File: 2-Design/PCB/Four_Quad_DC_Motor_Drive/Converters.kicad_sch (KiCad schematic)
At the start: 0 parts

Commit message: Added the SQL50 symbol and footprint
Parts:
- added U?: SQL50, symbol ee463_symbol_library:SQL50
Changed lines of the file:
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@@
 (kicad_sch (version 20211123) (generator eeschema)
   (paper "A4")
+  (symbol (lib_id "ee463_symbol_library:SQL50") (at 105.41 97.79 0) (unit 1)
+    (in_bom yes) (on_board yes) (fields_autoplaced)
+    (property "Reference" "U?" (id 0) (at 105.41 85.09 0))
+    (property "Value" "SQL50" (id 1) (at 105.41 87.63 0))
+    (property "Footprint" "" (id 2) (at 105.41 97.79 0)
+      (effects (font (size 1.27 1.27)) hide)
+    )
+    (property "Datasheet" "" (id 3) (at 105.41 97.79 0)
+      (effects (font (size 1.27 1.27)) hide)
+    )
+    (pin "1")
+    (pin "2")
+    (pin "3")
+    (pin "4")
+    (pin "5")
+  )
 )

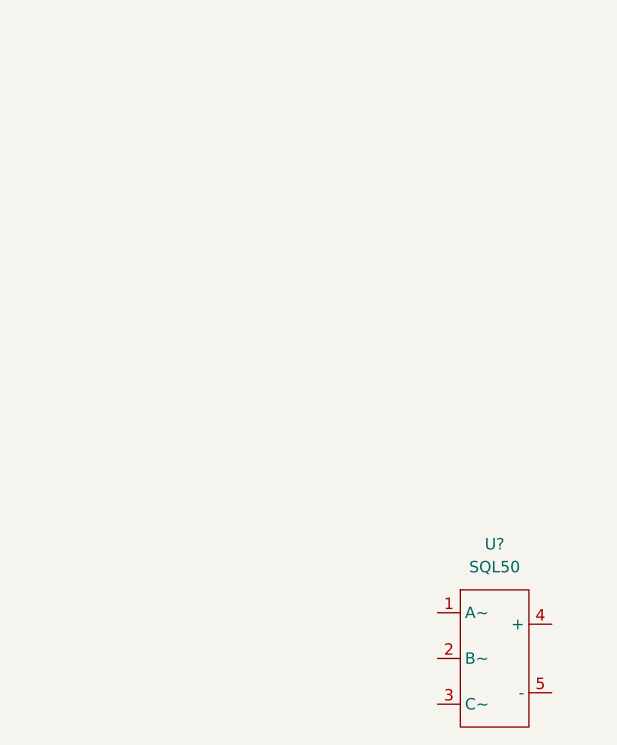
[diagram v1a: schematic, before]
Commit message: Added some more schematic symbols and three phase rectifier schematics
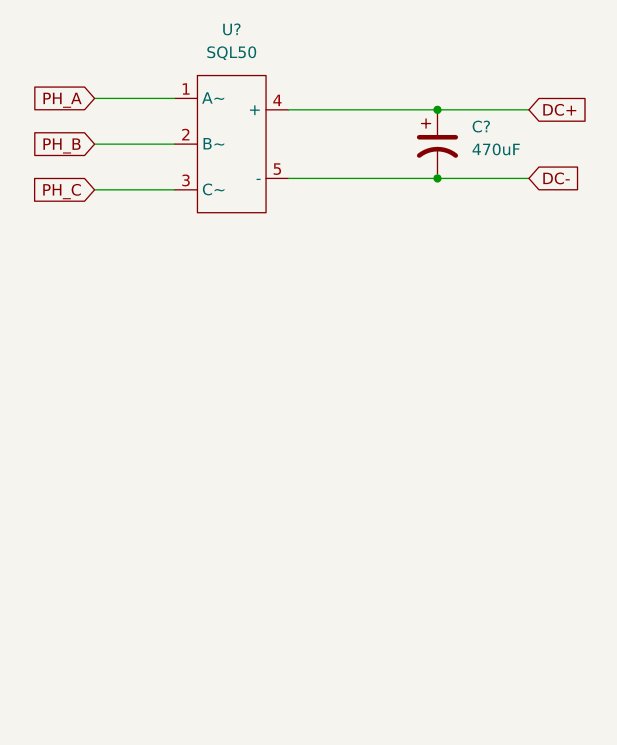
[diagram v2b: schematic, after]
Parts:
- added C?: 470uF, symbol Device:C_Polarized_US
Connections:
- net PH_A: now reaches U?.1 (A~)
- net PH_B: now reaches U?.2 (B~)
- net PH_C: now reaches U?.3 (C~)
- net DC+: now reaches U?.4 (+)
- net DC+: now also C?.1
- net DC-: now reaches U?.5 (-)
- net DC-: now also C?.2
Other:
- moved on the sheet: U?
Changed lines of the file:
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@@
 (kicad_sch (version 20211123) (generator eeschema)
   (paper "A4")
-  (symbol (lib_id "ee463_symbol_library:SQL50") (at 105.41 97.79 0) (unit 1)
+  (junction (at 99.06 36.83) (diameter 0) (color 0 0 0 0)
+  )
+  (junction (at 99.06 44.45) (diameter 0) (color 0 0 0 0)
+  )
+  (wire (pts (xy 60.96 45.72) (xy 69.85 45.72))
+    (stroke (width 0) (type default) (color 0 0 0 0))
+  )
+  (wire (pts (xy 82.55 44.45) (xy 99.06 44.45))
+    (stroke (width 0) (type default) (color 0 0 0 0))
+  )
+  (wire (pts (xy 99.06 36.83) (xy 109.22 36.83))
+    (stroke (width 0) (type default) (color 0 0 0 0))
+  )
+  (wire (pts (xy 60.96 35.56) (xy 69.85 35.56))
+    (stroke (width 0) (type default) (color 0 0 0 0))
+  )
+  (wire (pts (xy 99.06 44.45) (xy 109.22 44.45))
+    (stroke (width 0) (type default) (color 0 0 0 0))
+  )
+  (wire (pts (xy 82.55 36.83) (xy 99.06 36.83))
+    (stroke (width 0) (type default) (color 0 0 0 0))
+  )
+  (wire (pts (xy 60.96 40.64) (xy 69.85 40.64))
+    (stroke (width 0) (type default) (color 0 0 0 0))
+  )
+  (global_label "PH_C" (shape input) (at 60.96 45.72 180) (fields_autoplaced)
+    (effects (font (size 1.27 1.27)) (justify right))
+    (property "Intersheet References" "${INTERSHEET_REFS}" (id 0) (at 53.7088 45.6406 0)
+      (effects (font (size 1.27 1.27)) (justify right) hide)
+    )
+  )
+  (global_label "PH_A" (shape input) (at 60.96 35.56 180) (fields_autoplaced)
+    (effects (font (size 1.27 1.27)) (justify right))
+    (property "Intersheet References" "${INTERSHEET_REFS}" (id 0) (at 53.8902 35.4806 0)
+      (effects (font (size 1.27 1.27)) (justify right) hide)
+    )
+  )
+  (global_label "DC+" (shape input) (at 109.22 36.83 0) (fields_autoplaced)
+    (effects (font (size 1.27 1.27)) (justify left))
+    (property "Intersheet References" "${INTERSHEET_REFS}" (id 0) (at 115.7455 36.7506 0)
+      (effects (font (size 1.27 1.27)) (justify left) hide)
+    )
+  )
+  (global_label "DC-" (shape input) (at 109.22 44.45 0) (fields_autoplaced)
+    (effects (font (size 1.27 1.27)) (justify left))
+    (property "Intersheet References" "${INTERSHEET_REFS}" (id 0) (at 115.7455 44.3706 0)
+      (effects (font (size 1.27 1.27)) (justify left) hide)
+    )
+  )
+  (global_label "PH_B" (shape input) (at 60.96 40.64 180) (fields_autoplaced)
+    (effects (font (size 1.27 1.27)) (justify right))
+    (property "Intersheet References" "${INTERSHEET_REFS}" (id 0) (at 53.7088 40.5606 0)
+      (effects (font (size 1.27 1.27)) (justify right) hide)
+    )
+  )
+  (symbol (lib_id "Device:C_Polarized_US") (at 99.06 40.64 0) (unit 1)
     (in_bom yes) (on_board yes) (fields_autoplaced)
-    (property "Reference" "U?" (id 0) (at 105.41 85.09 0))
-    (property "Value" "SQL50" (id 1) (at 105.41 87.63 0))
-    (property "Footprint" "" (id 2) (at 105.41 97.79 0)
+    (property "Reference" "C?" (id 0) (at 102.87 38.7349 0)
+      (effects (font (size 1.27 1.27)) (justify left))
+    )
+    (property "Value" "470uF" (id 1) (at 102.87 41.2749 0)
+      (effects (font (size 1.27 1.27)) (justify left))
+    )
+    (property "Footprint" "" (id 2) (at 99.06 40.64 0)
       (effects (font (size 1.27 1.27)) hide)
     )
-    (property "Datasheet" "" (id 3) (at 105.41 97.79 0)
+    (property "Datasheet" "~" (id 3) (at 99.06 40.64 0)
       (effects (font (size 1.27 1.27)) hide)
     )
+    (pin "1")
+    (pin "2")
+  )
+  (symbol (lib_id "ee463_symbol_library:SQL50") (at 76.2 40.64 0) (unit 1)
+    (in_bom yes) (on_board yes) (fields_autoplaced)
+    (property "Reference" "U?" (id 0) (at 76.2 27.94 0))
+    (property "Value" "SQL50" (id 1) (at 76.2 30.48 0))
+    (property "Footprint" "" (id 2) (at 76.2 40.64 0)
+      (effects (font (size 1.27 1.27)) hide)
+    )
+    (property "Datasheet" "" (id 3) (at 76.2 40.64 0)
+      (effects (font (size 1.27 1.27)) hide)
+    )

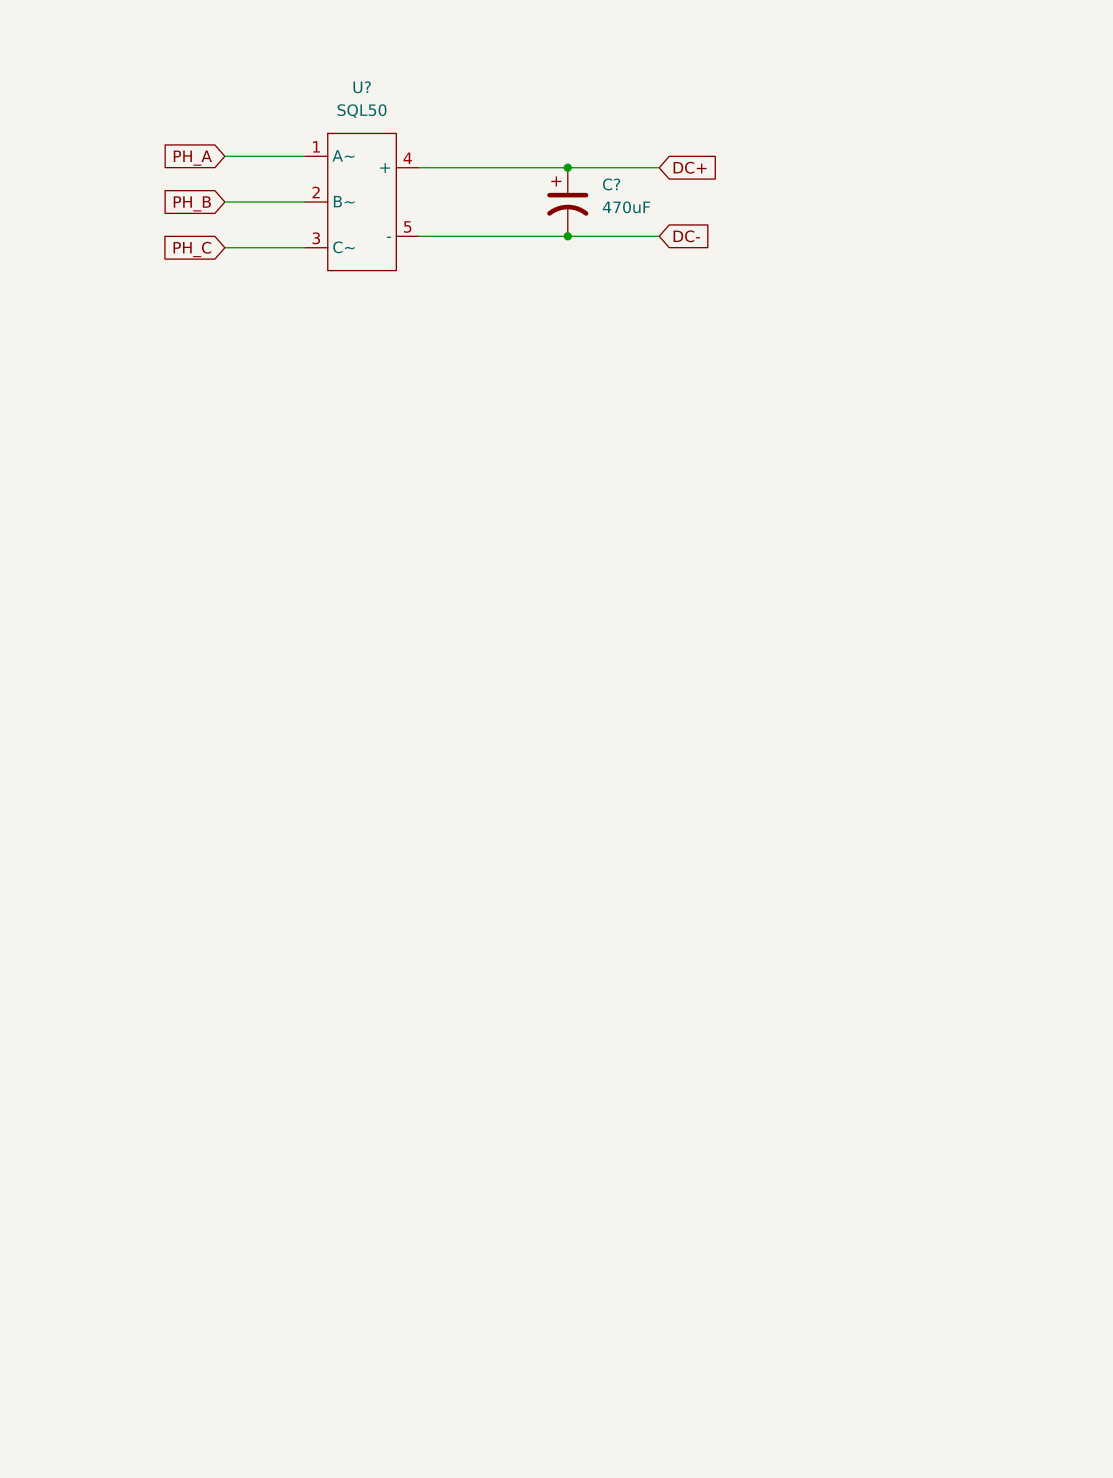
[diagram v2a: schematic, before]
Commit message: Changed the driver schematic, and added some schematic symbols
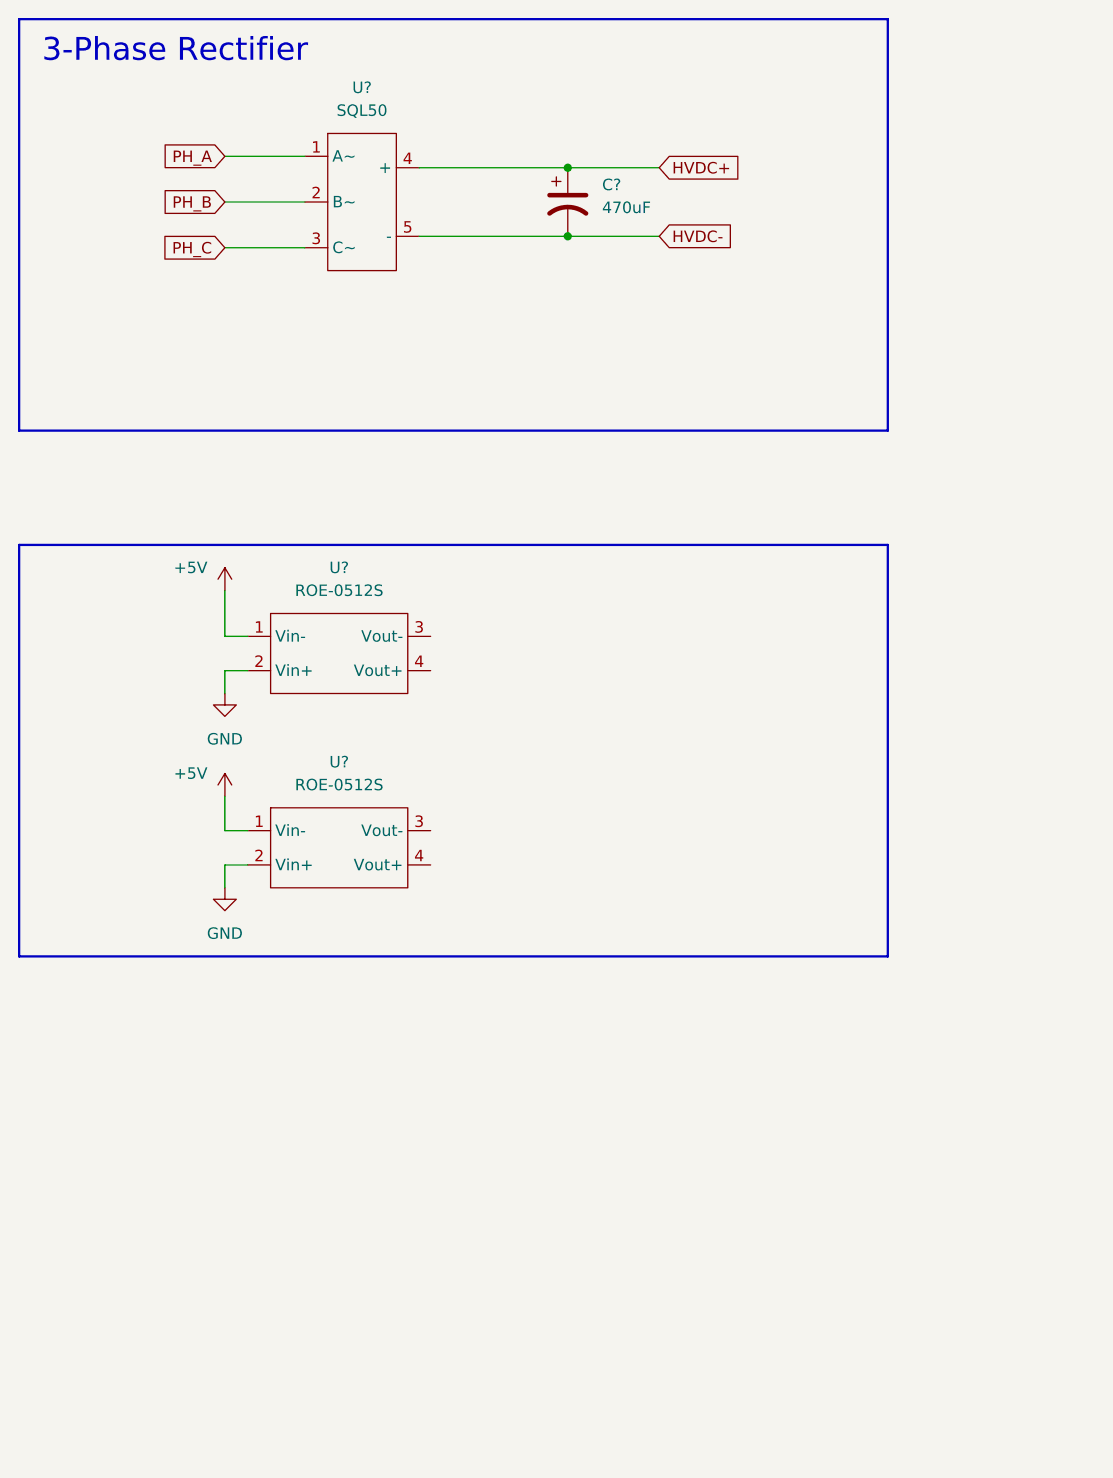
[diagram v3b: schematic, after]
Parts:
- added U? (x2): ROE-0512S, symbol ee463_symbol_library:ROE-0512S
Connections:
- net DC+ renamed HVDC+
- net DC- renamed HVDC-
- new net +5V: U?.1 (Vin-), U?.1 (Vin-)
- new net GND: U?.2 (Vin+), U?.2 (Vin+)
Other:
- note added: "3-Phase Rectifier"
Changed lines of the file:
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@@
+    (stroke (width 0) (type default) (color 0 0 0 0))
+  )
+  (polyline (pts (xy 134.62 124.46) (xy 38.1 124.46))
+    (stroke (width 0.254) (type solid) (color 132 0 0 1))
+  )
+  (wire (pts (xy 60.96 114.3) (xy 63.5 114.3))
+    (stroke (width 0) (type default) (color 0 0 0 0))
+  )
+  (wire (pts (xy 60.96 106.68) (xy 60.96 110.49))
     (stroke (width 0) (type default) (color 0 0 0 0))
   )
@@
     (stroke (width 0) (type default) (color 0 0 0 0))
   )
+  (wire (pts (xy 60.96 88.9) (xy 60.96 83.82))
+    (stroke (width 0) (type default) (color 0 0 0 0))
+  )
+  (polyline (pts (xy 134.62 66.04) (xy 38.1 66.04))
+    (stroke (width 0.254) (type solid) (color 132 0 0 1))
+  )
+  (polyline (pts (xy 38.1 20.32) (xy 134.62 20.32))
+    (stroke (width 0.254) (type solid) (color 132 0 0 1))
+  )
+  (wire (pts (xy 60.96 92.71) (xy 60.96 95.25))
+    (stroke (width 0) (type default) (color 0 0 0 0))
+  )
+  (polyline (pts (xy 134.62 78.74) (xy 134.62 124.46))
+    (stroke (width 0.254) (type solid) (color 132 0 0 1))
+  )
+  (polyline (pts (xy 38.1 78.74) (xy 134.62 78.74))
+    (stroke (width 0.254) (type solid) (color 132 0 0 1))
+  )
   (wire (pts (xy 60.96 35.56) (xy 69.85 35.56))
     (stroke (width 0) (type default) (color 0 0 0 0))
   )
+  (wire (pts (xy 60.96 114.3) (xy 60.96 116.84))
+    (stroke (width 0) (type default) (color 0 0 0 0))
+  )
+  (wire (pts (xy 63.5 92.71) (xy 60.96 92.71))
+    (stroke (width 0) (type default) (color 0 0 0 0))
+  )
+  (wire (pts (xy 60.96 110.49) (xy 63.5 110.49))
+    (stroke (width 0) (type default) (color 0 0 0 0))
+  )
   (wire (pts (xy 99.06 44.45) (xy 109.22 44.45))
     (stroke (width 0) (type default) (color 0 0 0 0))
@@
     (stroke (width 0) (type default) (color 0 0 0 0))
   )
+  (polyline (pts (xy 134.62 20.32) (xy 134.62 66.04))
+    (stroke (width 0.254) (type solid) (color 132 0 0 1))
+  )
+  (polyline (pts (xy 38.1 124.46) (xy 38.1 78.74))
+    (stroke (width 0.254) (type solid) (color 132 0 0 1))
+  )
+  (polyline (pts (xy 38.1 66.04) (xy 38.1 20.32))
+    (stroke (width 0.254) (type solid) (color 132 0 0 1))
+  )
   (wire (pts (xy 60.96 40.64) (xy 69.85 40.64))
     (stroke (width 0) (type default) (color 0 0 0 0))
+  )
+  (wire (pts (xy 63.5 88.9) (xy 60.96 88.9))
+    (stroke (width 0) (type default) (color 0 0 0 0))
+  )
+  (text "3-Phase Rectifier" (at 40.64 25.4 0)
+    (effects (font (size 2.54 2.54)) (justify left bottom))
   )
   (global_label "PH_C" (shape input) (at 60.96 45.72 180) (fields_autoplaced)
@@
     )
   )
-  (global_label "DC+" (shape input) (at 109.22 36.83 0) (fields_autoplaced)
+  (global_label "HVDC+" (shape input) (at 109.22 36.83 0) (fields_autoplaced)
     (effects (font (size 1.27 1.27)) (justify left))
-    (property "Intersheet References" "${INTERSHEET_REFS}" (id 0) (at 115.7455 36.7506 0)
+    (property "Intersheet References" "${INTERSHEET_REFS}" (id 0) (at 118.1645 36.7506 0)
       (effects (font (size 1.27 1.27)) (justify left) hide)
     )
   )
-  (global_label "DC-" (shape input) (at 109.22 44.45 0) (fields_autoplaced)
+  (global_label "HVDC-" (shape input) (at 109.22 44.45 0) (fields_autoplaced)
     (effects (font (size 1.27 1.27)) (justify left))
-    (property "Intersheet References" "${INTERSHEET_REFS}" (id 0) (at 115.7455 44.3706 0)
+    (property "Intersheet References" "${INTERSHEET_REFS}" (id 0) (at 118.1645 44.3706 0)
       (effects (font (size 1.27 1.27)) (justify left) hide)
     )
@@
     )
   )
+  (symbol (lib_id "ee463_symbol_library:ROE-0512S") (at 73.66 111.76 0) (unit 1)
+    (in_bom yes) (on_board yes) (fields_autoplaced)
+    (property "Reference" "U?" (id 0) (at 73.66 102.87 0))
+    (property "Value" "ROE-0512S" (id 1) (at 73.66 105.41 0))
+    (property "Footprint" "" (id 2) (at 73.66 111.76 0)
+      (effects (font (size 1.27 1.27)) hide)
+    )
+    (property "Datasheet" "" (id 3) (at 73.66 111.76 0)
+      (effects (font (size 1.27 1.27)) hide)
+    )
+    (pin "1")
+    (pin "2")
+    (pin "3")
+    (pin "4")
+  )
+  (symbol (lib_id "ee463_symbol_library:ROE-0512S") (at 73.66 90.17 0) (unit 1)
+    (in_bom yes) (on_board yes) (fields_autoplaced)
+    (property "Reference" "U?" (id 0) (at 73.66 81.28 0))
+    (property "Value" "ROE-0512S" (id 1) (at 73.66 83.82 0))
+    (property "Footprint" "" (id 2) (at 73.66 90.17 0)
+      (effects (font (size 1.27 1.27)) hide)
+    )
+    (property "Datasheet" "" (id 3) (at 73.66 90.17 0)
+      (effects (font (size 1.27 1.27)) hide)
+    )
+    (pin "1")
+    (pin "2")
+    (pin "3")
+    (pin "4")
+  )
+  (symbol (lib_id "power:+5V") (at 60.96 83.82 0) (unit 1)
+    (in_bom yes) (on_board yes)
+    (property "Reference" "#PWR?" (id 0) (at 60.96 87.63 0)
+      (effects (font (size 1.27 1.27)) hide)
+    )
+    (property "Value" "+5V" (id 1) (at 57.15 81.28 0))
+    (property "Footprint" "" (id 2) (at 60.96 83.82 0)
+      (effects (font (size 1.27 1.27)) hide)
+    )
+    (property "Datasheet" "" (id 3) (at 60.96 83.82 0)
+      (effects (font (size 1.27 1.27)) hide)
+    )
+    (pin "1")
+  )
   (symbol (lib_id "Device:C_Polarized_US") (at 99.06 40.64 0) (unit 1)
     (in_bom yes) (on_board yes) (fields_autoplaced)
@@
     (pin "1")
     (pin "2")
+  )
+  (symbol (lib_id "power:GND") (at 60.96 95.25 0) (unit 1)
+    (in_bom yes) (on_board yes) (fields_autoplaced)
+    (property "Reference" "#PWR?" (id 0) (at 60.96 101.6 0)
+      (effects (font (size 1.27 1.27)) hide)
+    )
+    (property "Value" "GND" (id 1) (at 60.96 100.33 0))
+    (property "Footprint" "" (id 2) (at 60.96 95.25 0)
+      (effects (font (size 1.27 1.27)) hide)
+    )
+    (property "Datasheet" "" (id 3) (at 60.96 95.25 0)
+      (effects (font (size 1.27 1.27)) hide)
+    )
+    (pin "1")
   )
   (symbol (lib_id "ee463_symbol_library:SQL50") (at 76.2 40.64 0) (unit 1)
@@
     (pin "5")
   )
+  (symbol (lib_id "power:GND") (at 60.96 116.84 0) (unit 1)
+    (in_bom yes) (on_board yes) (fields_autoplaced)
+    (property "Reference" "#PWR?" (id 0) (at 60.96 123.19 0)
+      (effects (font (size 1.27 1.27)) hide)
+    )
+    (property "Value" "GND" (id 1) (at 60.96 121.92 0))
+    (property "Footprint" "" (id 2) (at 60.96 116.84 0)
+      (effects (font (size 1.27 1.27)) hide)
+    )
+    (property "Datasheet" "" (id 3) (at 60.96 116.84 0)
+      (effects (font (size 1.27 1.27)) hide)
+    )
+    (pin "1")
+  )
+  (symbol (lib_id "power:+5V") (at 60.96 106.68 0) (unit 1)
+    (in_bom yes) (on_board yes)
+    (property "Reference" "#PWR?" (id 0) (at 60.96 110.49 0)
+      (effects (font (size 1.27 1.27)) hide)
+    )
+    (property "Value" "+5V" (id 1) (at 57.15 104.14 0))
+    (property "Footprint" "" (id 2) (at 60.96 106.68 0)
+      (effects (font (size 1.27 1.27)) hide)
+    )
+    (property "Datasheet" "" (id 3) (at 60.96 106.68 0)
+      (effects (font (size 1.27 1.27)) hide)
+    )
+    (pin "1")
+  )
 )
